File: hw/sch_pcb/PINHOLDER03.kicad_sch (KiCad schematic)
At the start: 11 parts, among them J1 HEADER_1x03, J2 HEADER_1x02, M1 HOLE, M2 HOLE, M3 HOLE, M4 HOLE

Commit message: Fix typo in the name. Cleanup layout.
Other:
- title: PINHOLDER02A -> PINHOLDER03A
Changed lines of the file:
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@@
   (paper "A4")
   (title_block
-    (title "PINHOLDER02A")
+    (title "PINHOLDER03A")
     (date "2023-04-12")
-    (rev "02A")
+    (rev "03A")
     (company "www.mlab.cz")
   )

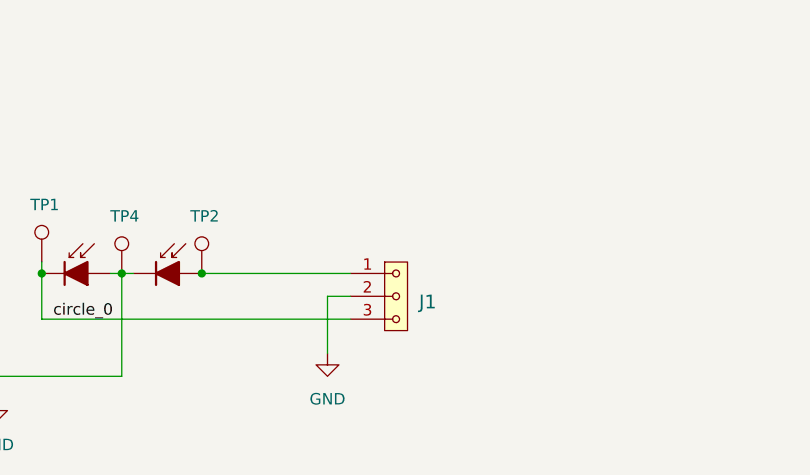
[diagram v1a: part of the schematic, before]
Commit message: zamena anoda-katoda diody
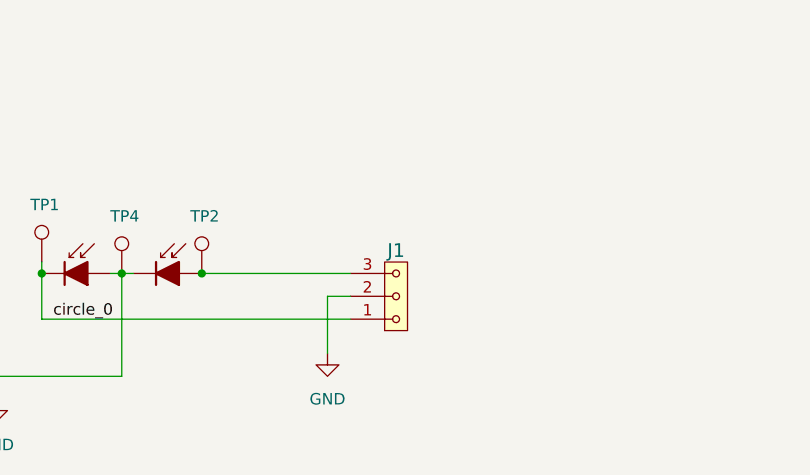
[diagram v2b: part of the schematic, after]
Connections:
- net circle_0: now also J1.1; no longer J1.3
- net at D2.2 (A), TP2.1: now also J1.3; no longer J1.1
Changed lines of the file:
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@@
     (pin "2")
   )
-  (symbol (lib_id "MLAB_HEADER:HEADER_1x03") (at 151.13 99.06 0) (unit 1)
+  (symbol (lib_id "MLAB_HEADER:HEADER_1x03") (at 151.13 99.06 0) (mirror x) (unit 1)
     (in_bom yes) (on_board yes) (fields_autoplaced)
-    (property "Reference" "J1" (id 0) (at 153.67 99.695 0)
-      (effects (font (size 1.524 1.524)) (justify left))
+    (property "Reference" "J1" (id 0) (at 151.13 93.98 0)
+      (effects (font (size 1.524 1.524)))
     )
-    (property "Value" "HEADER_1x03" (id 1) (at 153.67 101.6 0)
+    (property "Value" "HEADER_1x03" (id 1) (at 153.67 96.52 0)
       (effects (font (size 1.524 1.524)) (justify left) hide)
     )
-    (property "Footprint" "Connector_PinHeader_2.54mm:PinHeader_1x03_P2.54mm_Vertical_SMD_Pin1Left" (id 2) (at 151.13 96.52 0)
+    (property "Footprint" "Connector_PinHeader_2.54mm:PinHeader_1x03_P2.54mm_Vertical_SMD_Pin1Left" (id 2) (at 151.13 101.6 0)
       (effects (font (size 1.524 1.524)) hide)
     )
-    (property "Datasheet" "" (id 3) (at 151.13 96.52 0)
+    (property "Datasheet" "" (id 3) (at 151.13 101.6 0)
       (effects (font (size 1.524 1.524)))
     )

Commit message: text ve schematu
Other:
- note added: "A GND K"
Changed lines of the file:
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@@
     (stroke (width 0) (type solid) (color 0 0 0 0))
+  )
+  (text "A \nGND\nK" (at 153.67 101.6 0)
+    (effects (font (size 1.27 1.27)) (justify left bottom))
   )
   (text "MOUNTING HOLES" (at 255.27 31.75 0)
